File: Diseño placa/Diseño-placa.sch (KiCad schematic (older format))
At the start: 79 parts, among them IC1 ATMEGA32-P, M1 DIL24, M2 DIL24, M3 DIL16, P1 CONN_01X03, P2 CONN_02X08, P3 CONN_01X01, SW1 SW_PUSH, SW2 SW_PUSH, SW3 SW_PUSH, SW4 SW_PUSH, SW5 SW_PUSH, U1 REG104, U2 OPA625, U3 OPA625, U4 OPA625, U5 OPA625, U6 OPA625, U7 OPA625, X1 16M

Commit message: PCB
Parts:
- added C28: 10n, Capacitors_ThroughHole:C_Rect_L7_W6_P5, symbol C
- added P4: CONN_01X16, Pin_Headers:Pin_Header_Straight_1x16, symbol CONN_01X16
- added P5, P6: CONN_01X05, Pin_Headers:Pin_Header_Straight_1x05, symbol CONN_01X05
- added R31: 3.3k, Resistors_ThroughHole:Resistor_Horizontal_RM10mm, symbol R
- P2: footprint Pin_Headers:Pin_Header_Angled_1x16 -> Pin_Headers:Pin_Header_Angled_2x08
- SW1, SW2, SW3, SW4, SW5: footprint Buttons_Switches_ThroughHole:SW_PUSH -> Buttons_Switches_ThroughHole:SW_PUSH-12mm
- X1: footprint Crystals:Crystal_HC48-U_Vertical -> Crystals:Crystal_HC49-U_Vertical
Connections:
- net ADCIMPEDANCE: now also C28.1, R31.1; no longer C21.1, R28.1, U7.1
- net BDOWN: now also P5.2 (P2), P6.2 (P2)
- net BOK: now also P5.3 (P3), P6.3 (P3)
- net BUP: now also P5.1 (P1), P6.1 (P1)
- net GND: now also M3.1, M3.2, M3.3, M3.4, M3.5, P1.2 (P2), P1.3 (P3), C28.2, P4.1 (P1), P4.16 (P16), P5.5 (P5), P6.5 (P5)
- net LCDD0: now also P4.7 (P7)
- net LCDD1: now also P4.8 (P8)
- net LCDD2: now also P4.9 (P9)
- net LCDD3: now also P4.10 (P10)
- net LCDD4: now also P4.11 (P11)
- net LCDD5: now also P4.12 (P12)
- net LCDD6: now also P4.13 (P13)
- net LCDD7: now also P4.14 (P14)
- net LCDE: now also P4.6 (P6)
- net LCDRS: now also P4.4 (P4)
- net LCDRW: now also P4.5 (P5)
- net MUX2IO: no longer M3.3
- net VCC: now also P4.15 (P15), P4.2 (P2)
- net x120nA: no longer M3.2
- net x200nA: no longer M3.4
- net x30nA: no longer M3.1
- net x80nA: no longer M3.5
- net at C5.1, U1.4 (ENABLE), U1.5 (IN): now also P1.1 (P1); no longer P1.2 (P2)
- net POTE: now reaches DS1.3 (VO), RV1.2
- net POTE: now also P4.3 (P3)
- new net: C21.1, R28.1, R31.2, U7.1
- new net BSET: P5.4 (P4), P6.4 (P4)
- no-connect marks 5 -> 3
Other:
- moved on the sheet: P1
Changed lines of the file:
@@
 Text Label 7800 3550 0    60   ~ 0
 GND
-Text Label 11050 2950 2    60   ~ 0
+Text Label 11300 2950 2    60   ~ 0
 ADCIMPEDANCE
 Text Label 10900 4550 2    60   ~ 0
@@
 F 0 "X1" H 1100 2450 50  0000 C CNN
 F 1 "16M" H 1100 2150 50  0000 C CNN
-F 2 "Crystals:Crystal_HC48-U_Vertical" H 1100 2300 60  0001 C CNN
+F 2 "Crystals:Crystal_HC49-U_Vertical" H 1100 2300 60  0001 C CNN
 F 3 "" H 1100 2300 60  0000 C CNN
 	1    1100 2300
@@
 F 0 "SW1" H 1500 5960 50  0000 C CNN
 F 1 "SW_PUSH" H 1350 5770 50  0000 C CNN
-F 2 "Buttons_Switches_ThroughHole:SW_PUSH" H 1350 5850 60  0001 C CNN
+F 2 "Buttons_Switches_ThroughHole:SW_PUSH-12mm" H 1350 5850 60  0001 C CNN
 F 3 "" H 1350 5850 60  0000 C CNN
 	1    1350 5850
@@
 Text Label 3500 1700 0    60   ~ 0
 LCDE
-$Comp
-L SW_PUSH SW3
-U 1 1 56431899
-P 2750 5950
-F 0 "SW3" H 2900 6060 50  0000 C CNN
-F 1 "SW_PUSH" H 2750 5870 50  0000 C CNN
-F 2 "Buttons_Switches_ThroughHole:SW_PUSH" H 2750 5950 60  0001 C CNN
-F 3 "" H 2750 5950 60  0000 C CNN
-	1    2750 5950
-	1    0    0    -1
-$EndComp
 Text Label 2450 5950 2    60   ~ 0
 BDOWN
-Text Label 3050 5950 0    60   ~ 0
-GND
-$Comp
-L SW_PUSH SW2
-U 1 1 56431DBF
-P 2750 5600
-F 0 "SW2" H 2900 5710 50  0000 C CNN
-F 1 "SW_PUSH" H 2750 5520 50  0000 C CNN
-F 2 "Buttons_Switches_ThroughHole:SW_PUSH" H 2750 5600 60  0001 C CNN
-F 3 "" H 2750 5600 60  0000 C CNN
-	1    2750 5600
-	1    0    0    -1
-$EndComp
 Text Label 2450 5600 2    60   ~ 0
 BUP
-Text Label 3050 5600 0    60   ~ 0
-GND
-$Comp
-L SW_PUSH SW5
-U 1 1 56436066
-P 3850 5950
-F 0 "SW5" H 4000 6060 50  0000 C CNN
-F 1 "SW_PUSH" H 3850 5870 50  0000 C CNN
-F 2 "Buttons_Switches_ThroughHole:SW_PUSH" H 3850 5950 60  0001 C CNN
-F 3 "" H 3850 5950 60  0000 C CNN
-	1    3850 5950
-	1    0    0    -1
-$EndComp
 Text Label 3550 5950 2    60   ~ 0
 BESC
-Text Label 4150 5950 0    60   ~ 0
-GND
-$Comp
-L SW_PUSH SW4
-U 1 1 5643606F
-P 3850 5600
-F 0 "SW4" H 4000 5710 50  0000 C CNN
-F 1 "SW_PUSH" H 3850 5520 50  0000 C CNN
-F 2 "Buttons_Switches_ThroughHole:SW_PUSH" H 3850 5600 60  0001 C CNN
-F 3 "" H 3850 5600 60  0000 C CNN
-	1    3850 5600
-	1    0    0    -1
-$EndComp
 Text Label 3550 5600 2    60   ~ 0
 BOK
@@
 Text Label 6500 6050 2    60   ~ 0
 GND
-Text Label 6500 5350 2    60   ~ 0
-x30nA
-Text Label 6500 5450 2    60   ~ 0
-x120nA
-Text Label 6500 5650 2    60   ~ 0
-x200nA
-Text Label 6500 5750 2    60   ~ 0
-x80nA
 Text Label 7200 5450 0    60   ~ 0
 x120nA
@@
 Text Label 5850 6300 2    60   ~ 0
 MUX1IO
-Text Label 6500 5550 2    60   ~ 0
-MUX2IO
 Text Label 7200 5650 0    60   ~ 0
 MUX2IO
@@
 F 0 "P2" H 3400 7150 50  0000 C CNN
 F 1 "CONN_02X08" V 3400 6700 50  0000 C CNN
-F 2 "Pin_Headers:Pin_Header_Angled_1x16" H 3400 5500 60  0001 C CNN
+F 2 "Pin_Headers:Pin_Header_Angled_2x08" H 3400 5500 60  0001 C CNN
 F 3 "" H 3400 5500 60  0000 C CNN
 	1    3400 6700
@@
 L CONN_01X03 P1
 U 1 1 564DDDA7
-P 1100 6800
-F 0 "P1" H 1100 7000 50  0000 C CNN
-F 1 "CONN_01X03" V 1200 6800 50  0000 C CNN
-F 2 "Pin_Headers:Pin_Header_Straight_1x03" H 1100 6800 60  0001 C CNN
-F 3 "" H 1100 6800 60  0000 C CNN
-	1    1100 6800
-	-1   0    0    1
+P 1100 6900
+F 0 "P1" H 1100 7100 50  0000 C CNN
+F 1 "CONN_01X03" V 1200 6900 50  0000 C CNN
+F 2 "Pin_Headers:Pin_Header_Straight_1x03" H 1100 6900 60  0001 C CNN
+F 3 "" H 1100 6900 60  0000 C CNN
+	1    1100 6900
+	-1   0    0    -1
 $EndComp
 $Comp
@@
 	10550 2150 10750 2150
 Wire Wire Line
-	10350 2950 11050 2950
-Wire Wire Line
 	10450 3700 10450 3800
 Wire Wire Line
@@
 Wire Wire Line
 	7950 1700 8100 1700
-NoConn ~ 1300 6700
-NoConn ~ 1300 6900
 Wire Wire Line
 	4400 5200 4450 5200
 Text Label 4800 4800 2    60   ~ 0
 GND
+Text Label 6500 5350 2    60   ~ 0
+GND
+Text Label 6500 5450 2    60   ~ 0
+GND
+Text Label 6500 5550 2    60   ~ 0
+GND
+Text Label 6500 5650 2    60   ~ 0
+GND
+Text Label 6500 5750 2    60   ~ 0
+GND
+Wire Wire Line
+	1300 6900 1300 7200
+Wire Wire Line
+	1300 7200 1450 7200
+Connection ~ 1300 7000
+Text Label 3050 5950 0    60   ~ 0
+GND
+Text Label 3050 5600 0    60   ~ 0
+GND
+$Comp
+L SW_PUSH SW2
+U 1 1 56431DBF
+P 2750 5600
+F 0 "SW2" H 2900 5710 50  0000 C CNN
+F 1 "SW_PUSH" H 2750 5520 50  0000 C CNN
+F 2 "Buttons_Switches_ThroughHole:SW_PUSH-12mm" H 2750 5600 60  0001 C CNN
+F 3 "" H 2750 5600 60  0000 C CNN
+	1    2750 5600
+	1    0    0    -1
+$EndComp
+$Comp
+L SW_PUSH SW3
+U 1 1 56431899
+P 2750 5950
+F 0 "SW3" H 2900 6060 50  0000 C CNN
+F 1 "SW_PUSH" H 2750 5870 50  0000 C CNN
+F 2 "Buttons_Switches_ThroughHole:SW_PUSH-12mm" H 2750 5950 60  0001 C CNN
+F 3 "" H 2750 5950 60  0000 C CNN
+	1    2750 5950
+	1    0    0    -1
+$EndComp
+Text Label 4150 5950 0    60   ~ 0
+GND
+$Comp
+L SW_PUSH SW5
+U 1 1 56436066
+P 3850 5950
+F 0 "SW5" H 4000 6060 50  0000 C CNN
+F 1 "SW_PUSH" H 3850 5870 50  0000 C CNN
+F 2 "Buttons_Switches_ThroughHole:SW_PUSH-12mm" H 3850 5950 60  0001 C CNN
+F 3 "" H 3850 5950 60  0000 C CNN
+	1    3850 5950
+	1    0    0    -1
+$EndComp
+$Comp
+L SW_PUSH SW4
+U 1 1 5643606F
+P 3850 5600
+F 0 "SW4" H 4000 5710 50  0000 C CNN
+F 1 "SW_PUSH" H 3850 5520 50  0000 C CNN
+F 2 "Buttons_Switches_ThroughHole:SW_PUSH-12mm" H 3850 5600 60  0001 C CNN
+F 3 "" H 3850 5600 60  0000 C CNN
+	1    3850 5600
+	1    0    0    -1
+$EndComp
+$Comp
+L CONN_01X05 P6
+U 1 1 565442CE
+P 8400 4550
+F 0 "P6" H 8400 4850 50  0000 C CNN
+F 1 "CONN_01X05" V 8500 4550 50  0000 C CNN
+F 2 "Pin_Headers:Pin_Header_Straight_1x05" H 8400 4550 60  0001 C CNN
+F 3 "" H 8400 4550 60  0000 C CNN
+	1    8400 4550
+	1    0    0    -1
+$EndComp
+Text Label 8200 4350 2    60   ~ 0
+BUP
+Text Label 8200 4450 2    60   ~ 0
+BDOWN
+Text Label 8200 4550 2    60   ~ 0
+BOK
+Text Label 8200 4650 2    60   ~ 0
+BSET
+Text Label 8200 4750 2    60   ~ 0
+GND
+$Comp
+L CONN_01X05 P5
+U 1 1 56545169
+P 8400 3900
+F 0 "P5" H 8400 4200 50  0000 C CNN
+F 1 "CONN_01X05" V 8500 3900 50  0000 C CNN
+F 2 "Pin_Headers:Pin_Header_Straight_1x05" H 8400 3900 60  0001 C CNN
+F 3 "" H 8400 3900 60  0000 C CNN
+	1    8400 3900
+	1    0    0    -1
+$EndComp
+Text Label 8200 3700 2    60   ~ 0
+BUP
+Text Label 8200 3800 2    60   ~ 0
+BDOWN
+Text Label 8200 3900 2    60   ~ 0
+BOK
+Text Label 8200 4000 2    60   ~ 0
+BSET
+Text Label 8200 4100 2    60   ~ 0
+GND
+Text Label 7550 3750 2    60   ~ 0
+GND
+Text Label 7550 3850 2    60   ~ 0
+VCC
+Text Label 5000 4800 3    60   ~ 0
+POTE
+Text Label 7550 3950 2    60   ~ 0
+POTE
+Text Label 7550 4050 2    60   ~ 0
+LCDRS
+Text Label 7550 4150 2    60   ~ 0
+LCDRW
+Text Label 7550 4250 2    60   ~ 0
+LCDE
+Text Label 7550 4350 2    60   ~ 0
+LCDD0
+Text Label 7550 4450 2    60   ~ 0
+LCDD1
+Text Label 7550 4550 2    60   ~ 0
+LCDD2
+Text Label 7550 4650 2    60   ~ 0
+LCDD3
+Text Label 7550 4750 2    60   ~ 0
+LCDD4
+Text Label 7550 4850 2    60   ~ 0
+LCDD5
+Text Label 7550 4950 2    60   ~ 0
+LCDD6
+Text Label 7550 5050 2    60   ~ 0
+LCDD7
+$Comp
+L CONN_01X16 P4
+U 1 1 5654759B
+P 7750 4500
+F 0 "P4" H 7750 5350 50  0000 C CNN
+F 1 "CONN_01X16" V 7850 4500 50  0000 C CNN
+F 2 "Pin_Headers:Pin_Header_Straight_1x16" H 7750 4500 60  0001 C CNN
+F 3 "" H 7750 4500 60  0000 C CNN
+	1    7750 4500
+	1    0    0    -1
+$EndComp
+Text Label 7550 5150 2    60   ~ 0
+VCC
+Text Label 7550 5250 2    60   ~ 0
+GND
+$Comp
+L R R31
+U 1 1 56548EC9
+P 10500 2950
+F 0 "R31" V 10580 2950 50  0000 C CNN
+F 1 "3.3k" V 10500 2950 50  0000 C CNN
+F 2 "Resistors_ThroughHole:Resistor_Horizontal_RM10mm" V 10430 2950 30  0001 C CNN
+F 3 "" H 10500 2950 30  0000 C CNN
+	1    10500 2950
+	0    1    1    0
+$EndComp
+$Comp
+L C C28
+U 1 1 56548ECF
+P 10800 3200
+F 0 "C28" H 10825 3300 50  0000 L CNN
+F 1 "10n" H 10825 3100 50  0000 L CNN
+F 2 "Capacitors_ThroughHole:C_Rect_L7_W6_P5" H 10838 3050 30  0001 C CNN
+F 3 "" H 10800 3200 60  0000 C CNN
+	1    10800 3200
+	1    0    0    -1
+$EndComp
+Text Label 10800 3550 0    60   ~ 0
+GND
+Wire Wire Line
+	10800 3350 10800 3550
+Wire Wire Line
+	10650 2950 11300 2950
+Wire Wire Line
+	10800 3050 10800 2950
+Connection ~ 10800 2950
 $EndSCHEMATC

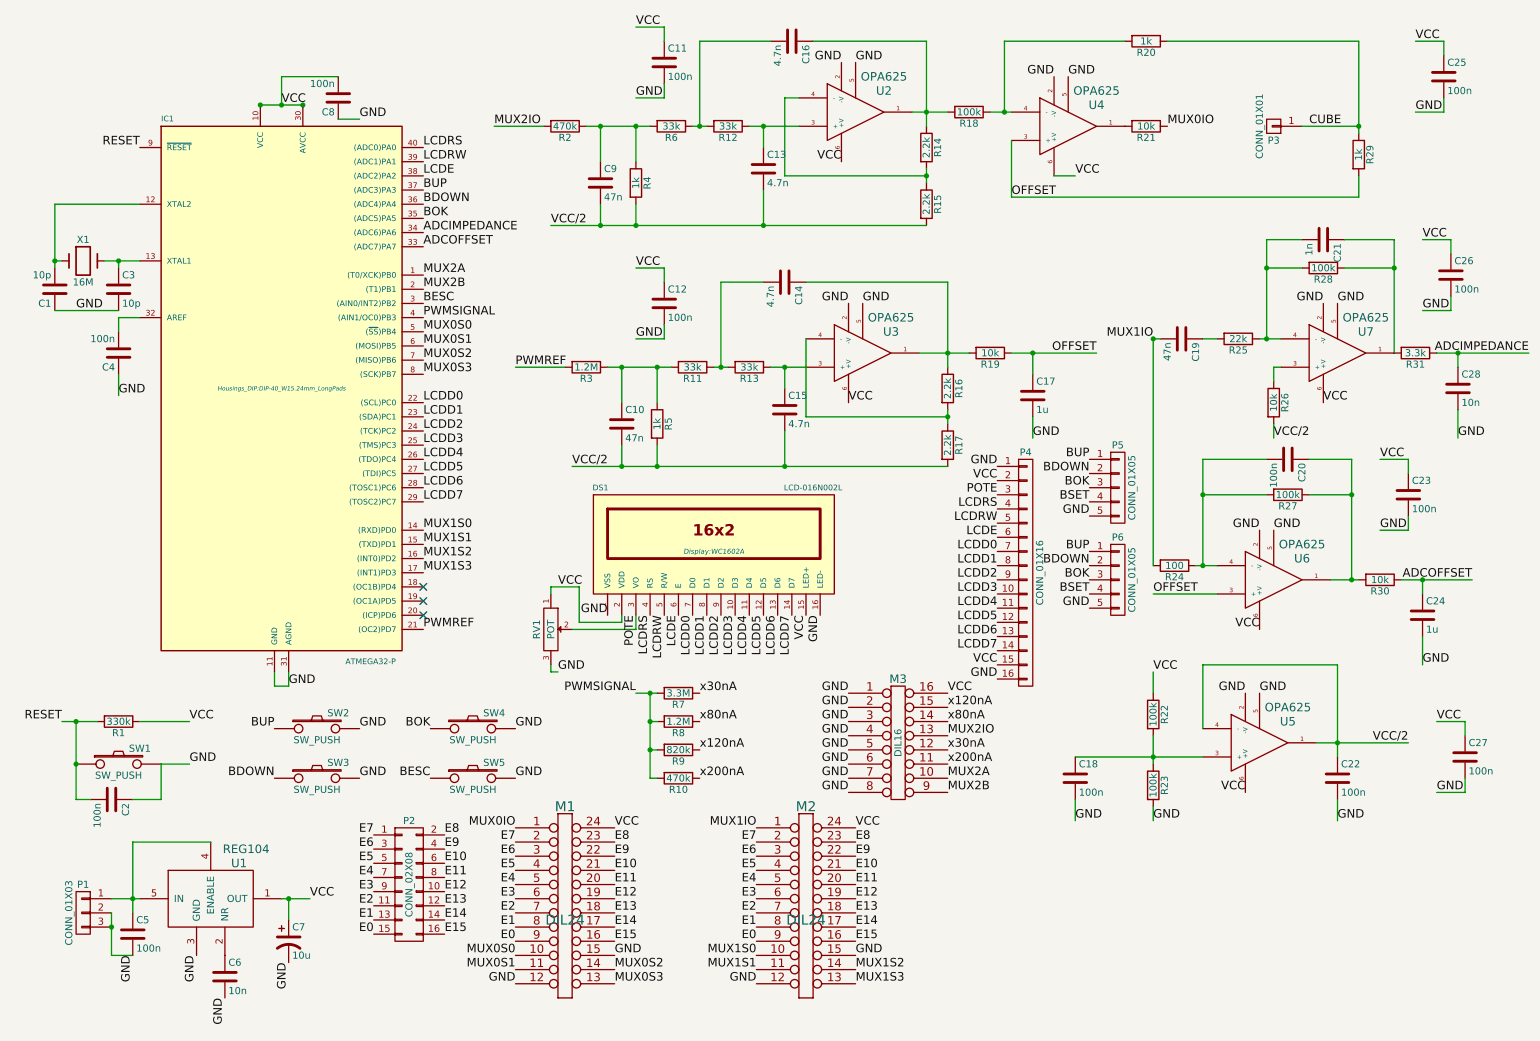
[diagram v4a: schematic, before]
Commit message: Actualización PCB
*Conector de programación
*Capacitores de los pulsadores
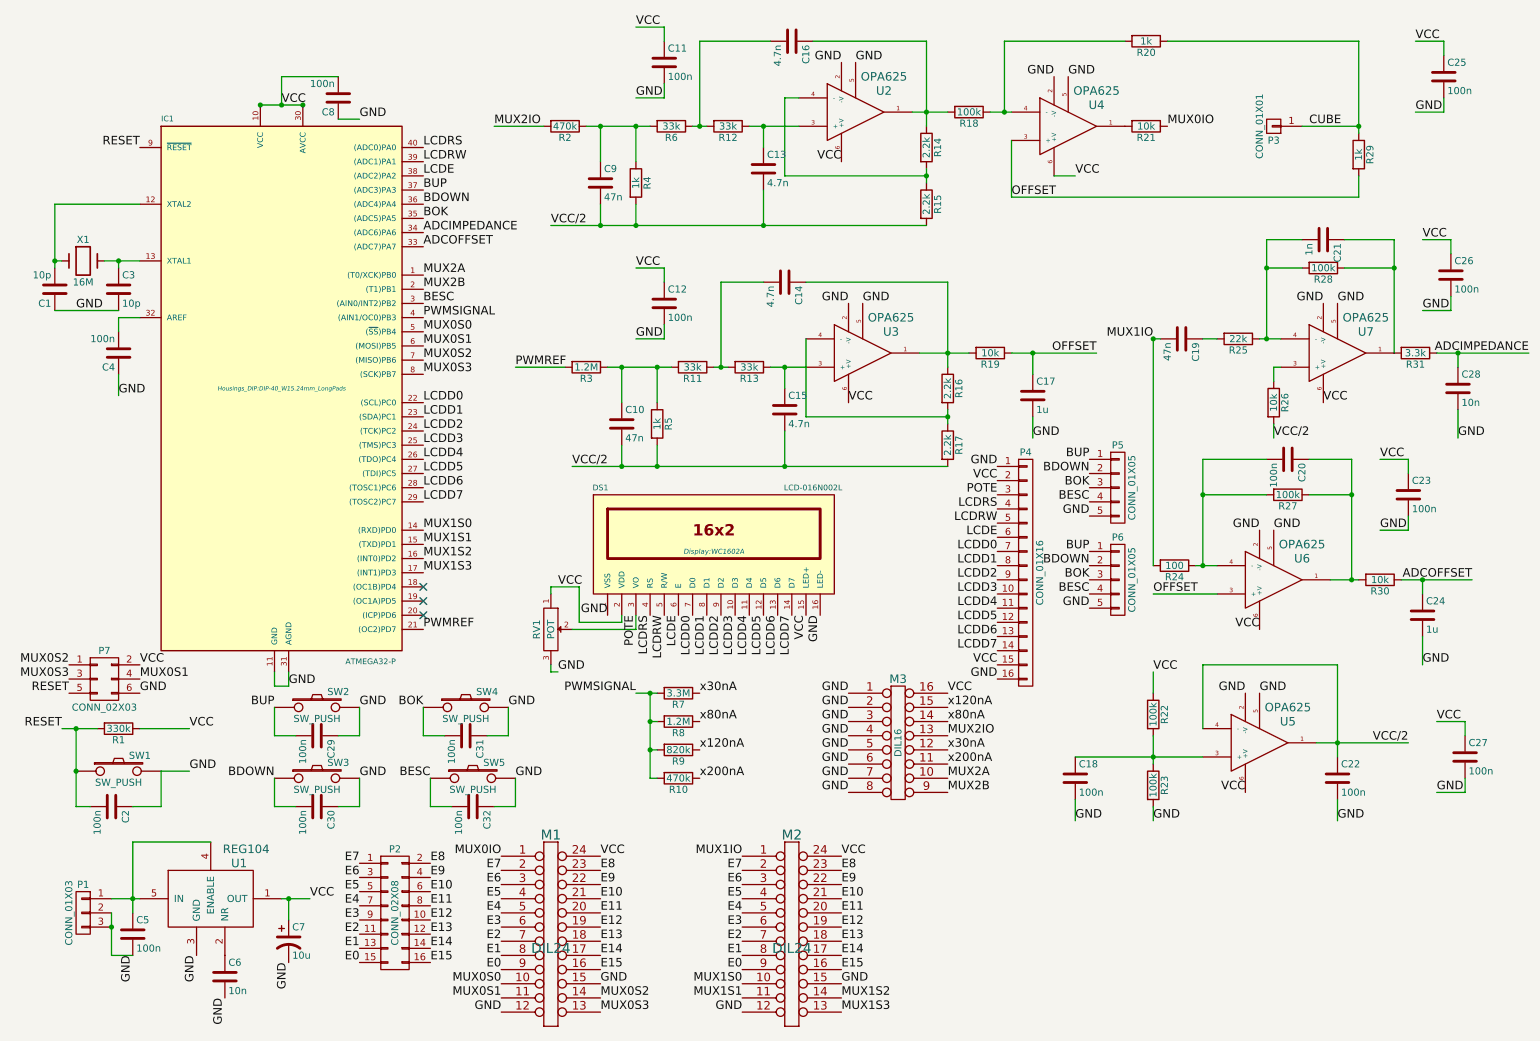
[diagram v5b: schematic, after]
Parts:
- added C29, C30, C31, C32: 100n, Capacitors_ThroughHole:C_Rect_L4_W2.5_P2.5, symbol C
- added P7: CONN_02X03, Pin_Headers:Pin_Header_Angled_2x03, symbol CONN_02X03
- U2, U3, U4, U5, U6, U7: footprint Housings_SOT-23_SOT-143_TSOT-6:SC-70-6 -> Housings_SOT-23_SOT-143_TSOT-6:TSOT-6-MK06A_Handsoldering
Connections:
- net BSET is gone; now on net BESC: P5.4 (P4), P6.4 (P4)
- net BDOWN: now also C30.2
- net BESC: now also C32.2
- net BOK: now also C31.2
- net BUP: now also C29.2
- net GND: now also C29.1, C30.1, C31.1, C32.1, P7.6 (P6)
- net MUX0S1: now also P7.4 (P4)
- net MUX0S2: now also P7.1 (P1)
- net MUX0S3: now also P7.3 (P3)
- net RESET: now also P7.5 (P5)
- net VCC: now also P7.2 (P2)
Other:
- moved on the sheet: C2, M1, M2, P2, R1, SW1, SW2, SW4

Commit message: PCB terminado
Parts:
- P1: footprint Pin_Headers:Pin_Header_Straight_1x03 -> varios:JACK_PWR
- P7: footprint Pin_Headers:Pin_Header_Angled_2x03 -> Pin_Headers:Pin_Header_Straight_2x03
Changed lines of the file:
@@
 F 0 "P1" H 1100 7100 50  0000 C CNN
 F 1 "CONN_01X03" V 1200 6900 50  0000 C CNN
-F 2 "Pin_Headers:Pin_Header_Straight_1x03" H 1100 6900 60  0001 C CNN
+F 2 "varios:JACK_PWR" H 1100 6900 60  0001 C CNN
 F 3 "" H 1100 6900 60  0000 C CNN
 	1    1100 6900
@@
 F 0 "P7" H 1250 5450 50  0000 C CNN
 F 1 "CONN_02X03" H 1250 5050 50  0000 C CNN
-F 2 "Pin_Headers:Pin_Header_Angled_2x03" H 1250 4050 60  0001 C CNN
+F 2 "Pin_Headers:Pin_Header_Straight_2x03" H 1250 4050 60  0001 C CNN
 F 3 "" H 1250 4050 60  0000 C CNN
 	1    1250 5250
